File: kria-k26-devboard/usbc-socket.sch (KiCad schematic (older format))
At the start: 8 parts, among them J10 USB4105-GF-A, Q11 DTC014TEBTL, Q15 PJA3441, U53 WE-TVS-82400152, U56 WE-TVS-82400152

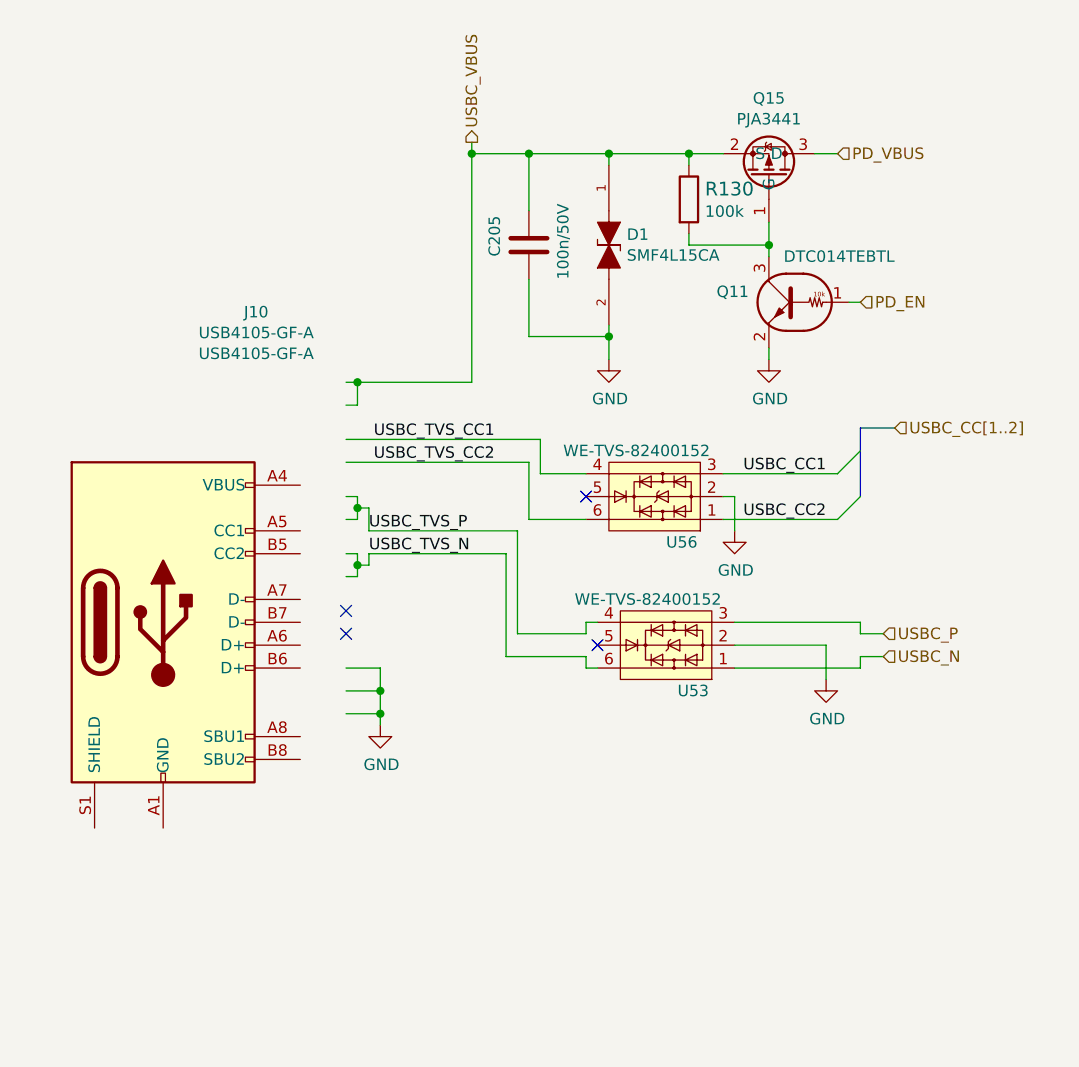
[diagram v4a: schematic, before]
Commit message: Finished Power planes and overall connectivity
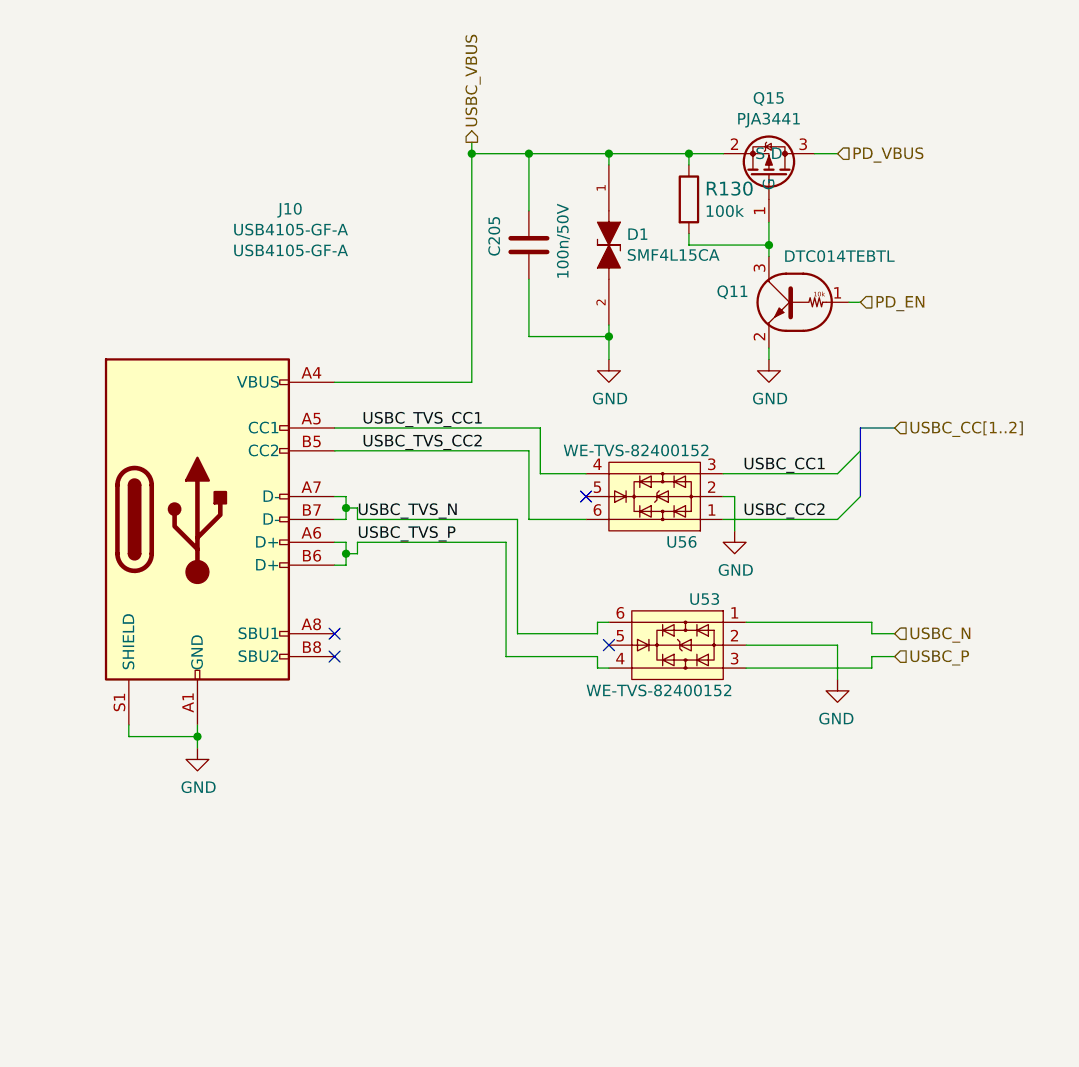
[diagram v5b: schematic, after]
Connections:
- wire segments 70 -> 65
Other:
- moved on the sheet: J10, U53
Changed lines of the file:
@@
 Comment4 ""
 $EndDescr
-Connection ~ 4600 4700
-Wire Wire Line
-	4600 4750 4600 4700
 $Comp
 L power:GND #PWR?
 U 1 1 62AA3664
-P 4600 4750
+P 3800 4850
 AR Path="/63C44BC2/62AA3664" Ref="#PWR?"  Part="1"
 AR Path="/63C44BC2/62A9ECDC/62AA3664" Ref="#PWR0374"  Part="1"
-F 0 "#PWR0374" H 4600 4500 50  0001 C CNN
-F 1 "GND" H 4605 4577 50  0000 C CNN
-F 2 "" H 4600 4750 50  0001 C CNN
-F 3 "" H 4600 4750 50  0001 C CNN
-	1    4600 4750
-	1    0    0    -1
-$EndComp
-Wire Wire Line
-	4600 4700 4450 4700
-Wire Wire Line
-	4600 4600 4600 4700
-Wire Wire Line
-	4450 4600 4600 4600
-Wire Wire Line
-	4500 4100 4450 4100
-Wire Wire Line
-	4450 4000 4500 4000
-Wire Wire Line
-	4500 3850 4450 3850
-Wire Wire Line
-	4450 3750 4500 3750
+F 0 "#PWR0374" H 3800 4600 50  0001 C CNN
+F 1 "GND" H 3805 4677 50  0000 C CNN
+F 2 "" H 3800 4850 50  0001 C CNN
+F 3 "" H 3800 4850 50  0001 C CNN
+	1    3800 4850
+	1    0    0    -1
+$EndComp
+Wire Wire Line
+	4450 3850 4400 3850
+Wire Wire Line
+	4400 3750 4450 3750
+Wire Wire Line
+	4450 4050 4400 4050
+Wire Wire Line
+	4400 3950 4450 3950
 $Comp
 L power:GND #PWR?
@@
 Wire Bus Line
 	6850 3450 6700 3450
-NoConn ~ 4450 4350
-NoConn ~ 4450 4250
+NoConn ~ 4400 4350
+NoConn ~ 4400 4450
 $Comp
 L antmicroCapacitorsmisc:C_100n_0402_50V C?
@@
 	6700 3550 6600 3650
 Wire Wire Line
-	4500 4000 4500 4050
-Wire Wire Line
-	4500 3750 4500 3800
-Wire Wire Line
-	4500 3800 4550 3800
-Connection ~ 4500 3800
-Wire Wire Line
-	4500 3800 4500 3850
-Wire Wire Line
-	6700 4450 6800 4450
-Connection ~ 4500 4050
-Wire Wire Line
-	4500 4050 4500 4100
-Text HLabel 6800 4350 2    50   Input ~ 0
+	4450 3750 4450 3800
+Wire Wire Line
+	4450 3950 4450 4000
+Wire Wire Line
+	4450 4000 4500 4000
+Connection ~ 4450 4000
+Wire Wire Line
+	4450 4000 4450 4050
+Wire Wire Line
+	6750 4350 6850 4350
+Connection ~ 4450 3800
+Wire Wire Line
+	4450 3800 4450 3850
+Text HLabel 6850 4450 2    50   Input ~ 0
 USBC_P
-Text HLabel 6800 4450 2    50   Input ~ 0
+Text HLabel 6850 4350 2    50   Input ~ 0
 USBC_N
 Wire Wire Line
@@
 L antmicroUSBDVIHDMIConnectors:USB4105-GF-A J?
 U 1 1 62AA367B
-P 3650 4300
+P 3800 3850
 AR Path="/63C44BC2/62AA367B" Ref="J?"  Part="1"
 AR Path="/63C44BC2/62A9ECDC/62AA367B" Ref="J10"  Part="1"
-F 0 "J10" H 4057 5657 50  0000 C CNN
-F 1 "USB4105-GF-A" H 4057 5566 50  0000 C CNN
-F 2 "antmicro-footprints:GCT_USB4105-GF-A" H 3000 4550 50  0001 L BNN
-F 3 "https://gct.co/files/drawings/usb4105.pdf" H 3650 4300 50  0001 L BNN
-F 4 "GCT" H 3000 4650 50  0001 L BNN "Manufacturer"
-F 5 "USB4105-GF-A" H 4057 5475 50  0000 C CNN "MPN"
-	1    3650 4300
+AR Path="/62AA367B" Ref="J10"  Part="1"
+F 0 "J10" H 4207 5207 50  0000 C CNN
+F 1 "USB4105-GF-A" H 4207 5116 50  0000 C CNN
+F 2 "antmicro-footprints:GCT_USB4105-GF-A" H 3150 4100 50  0001 L BNN
+F 3 "https://gct.co/files/drawings/usb4105.pdf" H 3800 3850 50  0001 L BNN
+F 4 "GCT" H 3150 4200 50  0001 L BNN "Manufacturer"
+F 5 "USB4105-GF-A" H 4207 5025 50  0000 C CNN "MPN"
+	1    3800 3850
 	1    0    0    -1
 $EndComp
@@
 Text Label 6550 3650 2    50   ~ 0
 USBC_CC1
-Wire Wire Line
-	4450 3350 4500 3350
-Wire Wire Line
-	4500 3350 4500 3250
-Wire Wire Line
-	4500 3250 4450 3250
-Wire Wire Line
-	4500 3250 5000 3250
-Connection ~ 4500 3250
 $Comp
 L antmicroTransistorsBipolarSingle:DTC014TEBTL Q11
@@
 L antmicroTVSDiodes:WE-TVS-82400152 U?
 U 1 1 62E99410
-P 5850 4400
+P 5900 4400
 AR Path="/625B0244/62E99410" Ref="U?"  Part="1"
 AR Path="/63C44BC2/62A9ECDC/62E99410" Ref="U53"  Part="1"
-F 0 "U53" H 5800 4600 50  0000 R CNN
-F 1 "WE-TVS-82400152" H 6250 4200 50  0000 R CNN
-F 2 "antmicro-footprints:SOT-563" H 5850 4200 50  0001 C CNN
-F 3 "https://katalog.we-online.de/pbs/datasheet/82400102.pdf" H 5850 4150 50  0001 C CNN
-F 4 "82400152" H 5500 4000 50  0001 C CNN "MPN"
-F 5 "Würth Elektronik" H 5600 4100 50  0001 C CNN "Manufacturer"
-	1    5850 4400
-	-1   0    0    1
-$EndComp
-Wire Wire Line
-	4500 4050 4550 4050
-NoConn ~ 5550 4400
+F 0 "U53" H 5850 4600 50  0000 R CNN
+F 1 "WE-TVS-82400152" H 6300 4200 50  0000 R CNN
+F 2 "antmicro-footprints:SOT-563" H 5900 4200 50  0001 C CNN
+F 3 "https://katalog.we-online.de/pbs/datasheet/82400102.pdf" H 5900 4150 50  0001 C CNN
+F 4 "82400152" H 5550 4000 50  0001 C CNN "MPN"
+F 5 "Würth Elektronik" H 5650 4100 50  0001 C CNN "Manufacturer"
+	1    5900 4400
+	-1   0    0    -1
+$EndComp
+Wire Wire Line
+	4450 3800 4500 3800
+NoConn ~ 5600 4400
 $Comp
 L power:GND #PWR?
 U 1 1 63812C2B
-P 6550 4550
+P 6600 4550
 AR Path="/63C44BC2/63812C2B" Ref="#PWR?"  Part="1"
 AR Path="/63C44BC2/62A9ECDC/63812C2B" Ref="#PWR0375"  Part="1"
-F 0 "#PWR0375" H 6550 4300 50  0001 C CNN
-F 1 "GND" H 6555 4377 50  0000 C CNN
-F 2 "" H 6550 4550 50  0001 C CNN
-F 3 "" H 6550 4550 50  0001 C CNN
-	1    6550 4550
-	1    0    0    -1
-$EndComp
-Wire Wire Line
-	6550 4400 6150 4400
-Wire Wire Line
-	6550 4400 6550 4550
-Wire Wire Line
-	6150 4500 6700 4500
-Wire Wire Line
-	6700 4500 6700 4450
-Wire Wire Line
-	6150 4300 6700 4300
-Wire Wire Line
-	6700 4300 6700 4350
-Wire Wire Line
-	6700 4350 6800 4350
-Text Label 4550 3900 0    50   ~ 0
+F 0 "#PWR0375" H 6600 4300 50  0001 C CNN
+F 1 "GND" H 6605 4377 50  0000 C CNN
+F 2 "" H 6600 4550 50  0001 C CNN
+F 3 "" H 6600 4550 50  0001 C CNN
+	1    6600 4550
+	-1   0    0    -1
+$EndComp
+Wire Wire Line
+	6600 4400 6200 4400
+Wire Wire Line
+	6600 4400 6600 4550
+Wire Wire Line
+	6200 4300 6750 4300
+Wire Wire Line
+	6750 4300 6750 4350
+Wire Wire Line
+	6200 4500 6750 4500
+Wire Wire Line
+	6750 4500 6750 4450
+Wire Wire Line
+	6750 4450 6850 4450
+Text Label 4500 3950 0    50   ~ 0
 USBC_TVS_P
 Wire Wire Line
-	4550 3800 4550 3900
-Wire Wire Line
-	4550 3900 5200 3900
-Wire Wire Line
-	4550 4050 4550 4000
-Text Label 4550 4000 0    50   ~ 0
+	4500 4000 4500 3950
+Wire Wire Line
+	4500 3950 5150 3950
+Wire Wire Line
+	4500 3800 4500 3850
+Text Label 4500 3850 0    50   ~ 0
 USBC_TVS_N
-Text Label 5100 3500 2    50   ~ 0
+Text Label 5050 3450 2    50   ~ 0
 USBC_TVS_CC1
-Text Label 5100 3600 2    50   ~ 0
+Text Label 5050 3550 2    50   ~ 0
 USBC_TVS_CC2
 $Comp
@@
 NoConn ~ 5500 3750
 Wire Wire Line
-	5150 4000 5150 4450
-Wire Wire Line
-	4550 4000 5150 4000
-Wire Wire Line
-	5250 3600 5250 3850
+	5250 3550 5250 3850
 Wire Wire Line
 	5250 3850 5500 3850
 Wire Wire Line
-	4450 3600 5250 3600
+	4400 3550 5250 3550
 Wire Wire Line
 	5500 3650 5300 3650
 Wire Wire Line
-	5300 3650 5300 3500
-Wire Wire Line
-	4450 3500 5300 3500
-Wire Wire Line
-	5200 4350 5500 4350
-Wire Wire Line
-	5500 4350 5500 4300
-Wire Wire Line
-	5500 4300 5550 4300
-Wire Wire Line
-	5500 4500 5500 4450
-Wire Wire Line
-	5500 4500 5550 4500
-Wire Wire Line
-	5200 3900 5200 4350
-Wire Wire Line
-	4450 4500 4600 4500
-Wire Wire Line
-	4600 4500 4600 4600
-Wire Wire Line
-	5150 4450 5500 4450
-Connection ~ 4600 4600
+	5300 3650 5300 3450
+Wire Wire Line
+	4400 3450 5300 3450
+Wire Wire Line
+	5550 4450 5550 4500
+Wire Wire Line
+	5550 4500 5600 4500
+Wire Wire Line
+	5550 4300 5550 4350
+Wire Wire Line
+	5550 4300 5600 4300
+Wire Wire Line
+	5200 4350 5550 4350
 $Comp
 L antmicroTVSDiodes:SMF4L15CA D1
@@
 	0    1    1    0
 $EndComp
+Wire Wire Line
+	4500 3850 5200 3850
+Wire Wire Line
+	5200 3850 5200 4350
+Wire Wire Line
+	5150 3950 5150 4450
+Wire Wire Line
+	5150 4450 5550 4450
+Wire Wire Line
+	4400 3250 5000 3250
+Wire Wire Line
+	3800 4750 3800 4800
+Wire Wire Line
+	3800 4800 3500 4800
+Wire Wire Line
+	3500 4800 3500 4750
 Wire Bus Line
 	6700 3450 6700 3750
+Connection ~ 3800 4800
+Wire Wire Line
+	3800 4800 3800 4850
 $EndSCHEMATC

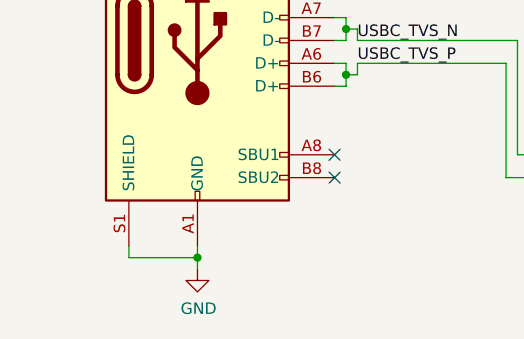
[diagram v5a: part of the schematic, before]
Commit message: Optimization of power planes, fixed missing capacitors on USB 3.0, unify shields, polishing of layout
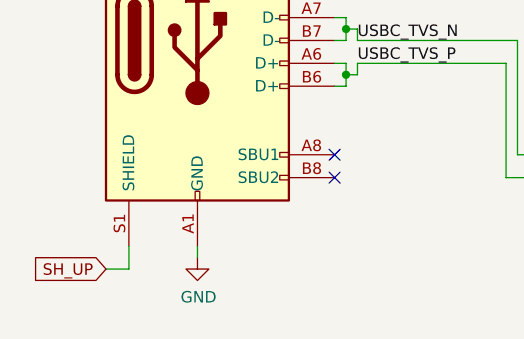
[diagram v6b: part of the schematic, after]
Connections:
- net GND: no longer J10.S1 (SHIELD)
- new net SH_UP: J10.S1 (SHIELD)
